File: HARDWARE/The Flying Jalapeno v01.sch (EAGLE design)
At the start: 79 parts, among them J1 ., J2 7V, Q1 8/16MHz, Q2 NPN, Q3 P-Channel MOSFET, Q4 NPN, Q5 P-Channel MOSFET, U1 ATMEGA328

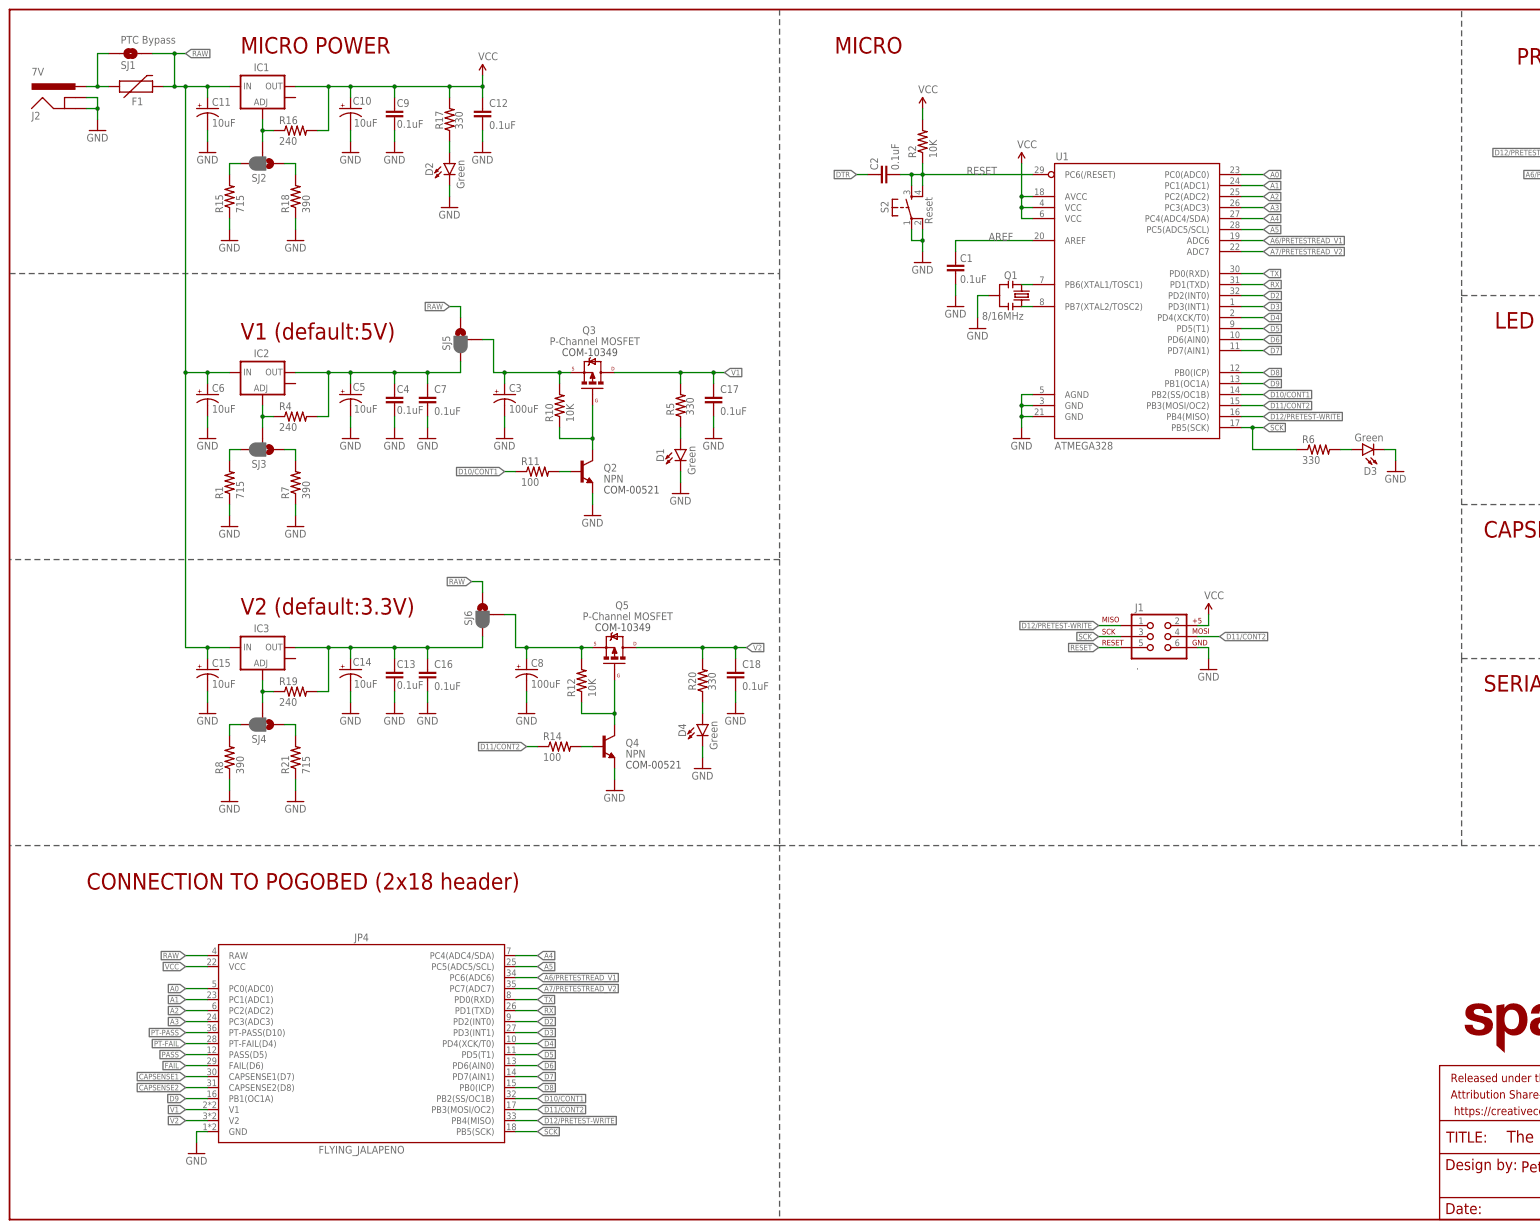
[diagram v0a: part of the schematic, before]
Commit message: Power input Diode
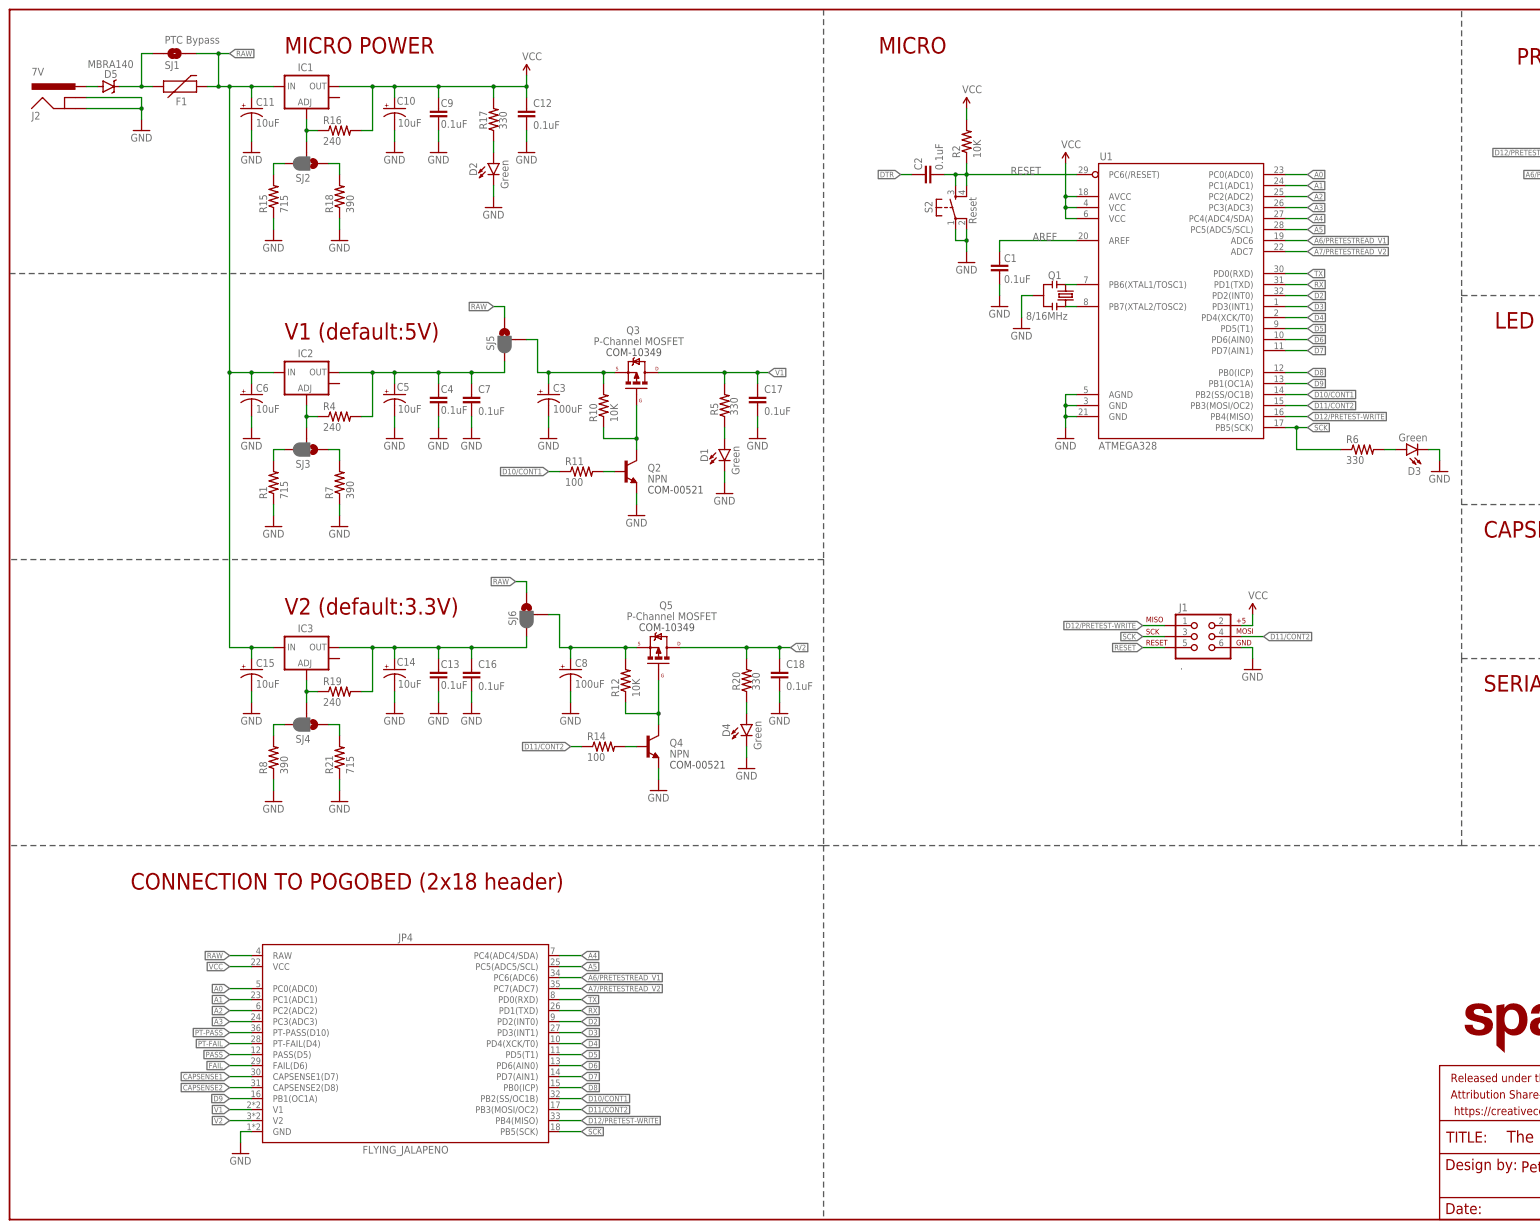
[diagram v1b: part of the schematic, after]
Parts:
- added D5: MBRA140, SparkFun-DiscreteSemi:DIODE-SCHOTTKY-MBRA140
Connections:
- new net N$24: D5.A, J2.PWR
- net N$15: now also D5.C; no longer J2.PWR
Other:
- moved on the sheet: C1, C10, C11, C12, C13, C14, C15, C16, C17, C18, C2, C3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

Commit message: Some PROD_IDS and moved to 100uF SMD caps
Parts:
- C1, C2: device SparkFun-Capacitors:0.1UF-25V-5%(0603) -> SparkFun-Capacitors:0.1UF-25V(+80/-20%)(0603)
- C10, C11, C14, C15, C5, C6: device SparkFun:CAP_POL1206 -> SparkFun-Capacitors:10UF-16V-10%(TANT)
- C12, C13, C16, C17, C18, C4, C7, C9: device SparkFun:CAP0603-CAP -> SparkFun-Capacitors:0.1UF-25V(+80/-20%)(0603)
- C3, C8: device SparkFun-Capacitors:CAP_POLPTH1 -> SparkFun-Capacitors:100UF-63V-20%(ELECT)
- J2: device SparkFun:POWER_JACKPTH_LOCK -> SparkFun-Connectors:POWER_JACKPTH_LOCK
- JP1: device SparkFun:ARDUINO_SERIAL_PROGRAMSMD -> SparkFun-Connectors:ARDUINO_SERIAL_PROGRAMSMD
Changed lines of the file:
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@@
 <part name="S2" library="SparkFun" deviceset="TAC_SWITCH" device="SMD" value="Reset"/>
 <part name="GND3" library="SparkFun" deviceset="GND" device=""/>
-<part name="C1" library="SparkFun-Capacitors" deviceset="0.1UF-25V-5%(0603)" device="" value="0.1uF"/>
+<part name="C1" library="SparkFun-Capacitors" deviceset="0.1UF-25V(+80/-20%)(0603)" device="" value="0.1uF"/>
 <part name="GND7" library="SparkFun" deviceset="GND" device=""/>
 <part name="R6" library="SparkFun-Resistors" deviceset="330OHM1/10W1%(0603)" device="" value="330"/>
@@
 <part name="P+1" library="SparkFun" deviceset="3.3V" device="" value="VCC"/>
 <part name="GND5" library="SparkFun" deviceset="GND" device=""/>
-<part name="JP1" library="SparkFun" deviceset="ARDUINO_SERIAL_PROGRAM" device="SMD" value="FTDI Basic"/>
-<part name="C2" library="SparkFun-Capacitors" deviceset="0.1UF-25V-5%(0603)" device="" value="0.1uF"/>
+<part name="JP1" library="SparkFun-Connectors" deviceset="ARDUINO_SERIAL_PROGRAM" device="SMD" value="FTDI Basic"/>
+<part name="C2" library="SparkFun-Capacitors" deviceset="0.1UF-25V(+80/-20%)(0603)" device="" value="0.1uF"/>
 <part name="JP5" library="SparkFun" deviceset="FIDUCIAL" device="UFIDUCIAL"/>
 <part name="J1" library="SparkFun" deviceset="AVR_SPI_PRG_6" device="2X3_LOCK" value="."/>
@@
 <part name="GND15" library="SparkFun" deviceset="GND" device=""/>
 <part name="Q3" library="Testing" deviceset="MOSFET-PCHANNEL" device="PTH" value="P-Channel MOSFET"/>
-<part name="C3" library="SparkFun-Capacitors" deviceset="CAP_POL" device="PTH1" value="100uF"/>
+<part name="C3" library="SparkFun-Capacitors" deviceset="100UF-63V-20%(ELECT)" device="" value="100uF"/>
 <part name="GND16" library="SparkFun" deviceset="GND" device=""/>
 <part name="Q4" library="SparkFun" deviceset="TRANSISTOR_NPN" device="SOT23" value="NPN"/>
@@
 <part name="GND17" library="SparkFun" deviceset="GND" device=""/>
 <part name="Q5" library="Testing" deviceset="MOSFET-PCHANNEL" device="PTH" value="P-Channel MOSFET"/>
-<part name="C8" library="SparkFun-Capacitors" deviceset="CAP_POL" device="PTH1" value="100uF"/>
+<part name="C8" library="SparkFun-Capacitors" deviceset="100UF-63V-20%(ELECT)" device="" value="100uF"/>
 <part name="GND18" library="SparkFun" deviceset="GND" device=""/>
 <part name="FRAME1" library="SparkFun-Aesthetics" deviceset="FRAME-LEDGER" device=""/>
 <part name="F1" library="Testing" deviceset="PTC" device="WIDE" value=""/>
-<part name="J2" library="SparkFun" deviceset="POWER_JACK" device="PTH_LOCK" value="7V"/>
+<part name="J2" library="SparkFun-Connectors" deviceset="POWER_JACK" device="PTH_LOCK" value="7V"/>
 <part name="GND19" library="SparkFun" deviceset="GND" device=""/>
 <part name="SJ1" library="SparkFun-Passives" deviceset="JUMPER-PAD-2-NO" device="" value="PTC Bypass"/>
 <part name="GND20" library="SparkFun" deviceset="GND" device=""/>
 <part name="P+3" library="SparkFun" deviceset="3.3V" device="" value="VCC"/>
-<part name="C9" library="SparkFun" deviceset="CAP" device="0603-CAP" value="0.1uF"/>
-<part name="C10" library="SparkFun" deviceset="CAP_POL" device="1206" value="10uF"/>
+<part name="C9" library="SparkFun-Capacitors" deviceset="0.1UF-25V(+80/-20%)(0603)" device="" value="0.1uF"/>
+<part name="C10" library="SparkFun-Capacitors" deviceset="10UF-16V-10%(TANT)" device="" value="10uF"/>
 <part name="GND21" library="SparkFun" deviceset="GND" device=""/>
 <part name="GND22" library="SparkFun" deviceset="GND" device=""/>
 <part name="P+5" library="SparkFun" deviceset="VCC" device=""/>
-<part name="C11" library="SparkFun" deviceset="CAP_POL" device="1206" value="10uF"/>
+<part name="C11" library="SparkFun-Capacitors" deviceset="10UF-16V-10%(TANT)" device="" value="10uF"/>
 <part name="IC1" library="SparkFun" deviceset="V_REG_LM1117" device="SOT223"/>
 <part name="R15" library="SparkFun" deviceset="RESISTOR" device="0603-RES" value="715"/>
@@
 <part name="R17" library="SparkFun-Resistors" deviceset="330OHM1/10W1%(0603)" device="" value="330"/>
 <part name="R18" library="SparkFun-Resistors" deviceset="390OHM1/10W1%(0603)" device="" value="390"/>
-<part name="C12" library="SparkFun" deviceset="CAP" device="0603-CAP" value="0.1uF"/>
+<part name="C12" library="SparkFun-Capacitors" deviceset="0.1UF-25V(+80/-20%)(0603)" device="" value="0.1uF"/>
 <part name="GND25" library="SparkFun" deviceset="GND" device=""/>
 <part name="SJ2" library="SparkFun-Passives" deviceset="JUMPER-PAD-3-2OF3_NC_BY_PASTE" device="" value=""/>
 <part name="GND26" library="SparkFun" deviceset="GND" device=""/>
 <part name="GND27" library="SparkFun" deviceset="GND" device=""/>
-<part name="C4" library="SparkFun" deviceset="CAP" device="0603-CAP" value="0.1uF"/>
-<part name="C5" library="SparkFun" deviceset="CAP_POL" device="1206" value="10uF"/>
+<part name="C4" library="SparkFun-Capacitors" deviceset="0.1UF-25V(+80/-20%)(0603)" device="" value="0.1uF"/>
+<part name="C5" library="SparkFun-Capacitors" deviceset="10UF-16V-10%(TANT)" device="" value="10uF"/>
 <part name="GND2" library="SparkFun" deviceset="GND" device=""/>
 <part name="GND6" library="SparkFun" deviceset="GND" device=""/>
-<part name="C6" library="SparkFun" deviceset="CAP_POL" device="1206" value="10uF"/>
+<part name="C6" library="SparkFun-Capacitors" deviceset="10UF-16V-10%(TANT)" device="" value="10uF"/>
 <part name="IC2" library="SparkFun" deviceset="V_REG_LM1117" device="SOT223"/>
 <part name="R1" library="SparkFun" deviceset="RESISTOR" device="0603-RES" value="715"/>
@@
 <part name="R5" library="SparkFun-Resistors" deviceset="330OHM1/10W1%(0603)" device="" value="330"/>
 <part name="R7" library="SparkFun-Resistors" deviceset="390OHM1/10W1%(0603)" device="" value="390"/>
-<part name="C7" library="SparkFun" deviceset="CAP" device="0603-CAP" value="0.1uF"/>
+<part name="C7" library="SparkFun-Capacitors" deviceset="0.1UF-25V(+80/-20%)(0603)" device="" value="0.1uF"/>
 <part name="GND11" library="SparkFun" deviceset="GND" device=""/>
 <part name="SJ3" library="SparkFun-Passives" deviceset="JUMPER-PAD-3-2OF3_NC_BY_PASTE" device="" value=""/>
 <part name="GND12" library="SparkFun" deviceset="GND" device=""/>
 <part name="GND13" library="SparkFun" deviceset="GND" device=""/>
-<part name="C13" library="SparkFun" deviceset="CAP" device="0603-CAP" value="0.1uF"/>
-<part name="C14" library="SparkFun" deviceset="CAP_POL" device="1206" value="10uF"/>
+<part name="C13" library="SparkFun-Capacitors" deviceset="0.1UF-25V(+80/-20%)(0603)" device="" value="0.1uF"/>
+<part name="C14" library="SparkFun-Capacitors" deviceset="10UF-16V-10%(TANT)" device="" value="10uF"/>
 <part name="GND28" library="SparkFun" deviceset="GND" device=""/>
 <part name="GND29" library="SparkFun" deviceset="GND" device=""/>
-<part name="C15" library="SparkFun" deviceset="CAP_POL" device="1206" value="10uF"/>
+<part name="C15" library="SparkFun-Capacitors" deviceset="10UF-16V-10%(TANT)" device="" value="10uF"/>
 <part name="IC3" library="SparkFun" deviceset="V_REG_LM1117" device="SOT223"/>
 <part name="R8" library="SparkFun" deviceset="RESISTOR" device="0603-RES" value="390"/>
@@
 <part name="R20" library="SparkFun-Resistors" deviceset="330OHM1/10W1%(0603)" device="" value="330"/>
 <part name="R21" library="SparkFun-Resistors" deviceset="390OHM1/10W1%(0603)" device="" value="715"/>
-<part name="C16" library="SparkFun" deviceset="CAP" device="0603-CAP" value="0.1uF"/>
+<part name="C16" library="SparkFun-Capacitors" deviceset="0.1UF-25V(+80/-20%)(0603)" device="" value="0.1uF"/>
 <part name="GND32" library="SparkFun" deviceset="GND" device=""/>
 <part name="SJ4" library="SparkFun-Passives" deviceset="JUMPER-PAD-3-2OF3_NC_BY_PASTE" device="" value=""/>
@@
 <part name="GND35" library="SparkFun" deviceset="GND" device=""/>
 <part name="LOGO1" library="SparkFun-Aesthetics" deviceset="SFE_LOGO_NAME_FLAME" device=".5_INCH" value="SFE_LOGO_NAME_FLAME.5_INCH"/>
-<part name="C17" library="SparkFun" deviceset="CAP" device="0603-CAP" value="0.1uF"/>
+<part name="C17" library="SparkFun-Capacitors" deviceset="0.1UF-25V(+80/-20%)(0603)" device="" value="0.1uF"/>
 <part name="GND36" library="SparkFun" deviceset="GND" device=""/>
-<part name="C18" library="SparkFun" deviceset="CAP" device="0603-CAP" value="0.1uF"/>
+<part name="C18" library="SparkFun-Capacitors" deviceset="0.1UF-25V(+80/-20%)(0603)" device="" value="0.1uF"/>
 <part name="GND37" library="SparkFun" deviceset="GND" device=""/>
 <part name="LOGO3" library="SparkFun-Aesthetics" deviceset="SFE_LOGO_FLAME" device=".1_INCH"/>

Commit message: more PROD_IDs
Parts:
- removed S2: Reset, SparkFun:TAC_SWITCHSMD
- removed U1: ATMEGA328, SparkFun:ATMEGA168
- added S1: SWITCH-MOMENTARY-2SMD-REDUNDANT, SparkFun-Electromechanical:SWITCH-MOMENTARY-2SMD-REDUNDANT
- added U2: ATMEGA328P_TQFP, SparkFun-DigitalIC:ATMEGA328P_TQFP
- D1, D2, D3, D4: value Green -> RED; device SparkFun-LED:LED1206 -> SparkFun-LED:LED-RED1206
- F1: value PTCWIDE -> PTCTHERMISTOR1206; device Testing:PTCWIDE -> SparkFun-PowerIC:PTCTHERMISTOR1206
- IC1, IC2, IC3: device SparkFun:V_REG_LM1117SOT223 -> SparkFun-PowerIC:V_REG_LM1117SOT223
- Q1: value 8/16MHz -> 16MHZ; device Testing:RESONATOR1:1 -> SparkFun-FreqCtrl:RESONATOR16MHZ
- Q2, Q4: value NPN -> MMBT2222A; device SparkFun:TRANSISTOR_NPNSOT23 -> SparkFun-DiscreteSemi:TRANSISTOR_NPNMMBT2222A
- R1, R15: device SparkFun:RESISTOR0603-RES -> SparkFun-Resistors:715OHM1/10W1%(0603)
- R10, R12: device SparkFun:RESISTOR0603-RES -> SparkFun-Resistors:10KOHM-1/10W-1%(0603)0603
- R11, R14: device SparkFun:RESISTOR0603-RES -> SparkFun-Resistors:100OHM-1/10W-1%(0603)
- R13, R28, R3, R30: device Testing:RESISTOR0603-RES -> SparkFun-Resistors:10KOHM-1/10W-1%(0603)0603
- R16, R19, R4: device SparkFun:RESISTOR0603-RES -> SparkFun-Resistors:240OHM1/10W1%(0603)
- R17, R20, R22, R23, R24, R25, R5, R6: value 330 -> 390; device SparkFun-Resistors:330OHM1/10W1%(0603) -> SparkFun-Resistors:390OHM1/10W1%(0603)
- R2: device SparkFun-Resistors:10KOHM1/10W1%(0603)0603 -> SparkFun-Resistors:10KOHM-1/10W-1%(0603)0603
- R21: device SparkFun-Resistors:390OHM1/10W1%(0603) -> SparkFun-Resistors:715OHM1/10W1%(0603)
- R26, R27: value 20M -> 22M ohm
- R29, R9: value 100K -> 100k; device Testing:RESISTOR0603-RES -> SparkFun-Resistors:100KOHM-1/10W-1%(0603)
- R8: device SparkFun:RESISTOR0603-RES -> SparkFun-Resistors:390OHM1/10W1%(0603)
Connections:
- removed net N$25: C13.1, C14.+, C16.1, IC3.OUT, R19.2, SJ6.3
- new net VREG2OUT: C13.1, C14.+, C16.1, IC3.OUT, IC3.OUT@1, R19.2, SJ6.3
- net A0: now also U2.PC0(ADC0); no longer U1.PC0(ADC0)
- net A1: now also U2.PC1(ADC1); no longer U1.PC1(ADC1)
- net A2: now also U2.PC2(ADC2); no longer U1.PC2(ADC2)
- net A3: now also U2.PC3(ADC3); no longer U1.PC3(ADC3)
- net A4: now also U2.PC4(ADC4/SDA); no longer U1.PC4(ADC4/SDA)
- net A5: now also U2.PC5(ADC5/SCL); no longer U1.PC5(ADC5/SCL)
- net A6/PRETESTREAD_V1: now also U2.ADC6; no longer U1.ADC6
- net A7/PRETESTREAD_V2: now also U2.ADC7; no longer U1.ADC7
- net AREF: now also U2.AREF; no longer U1.AREF
- net D10/CONT1: now also U2.PB2(SS/OC1B); no longer U1.PB2(SS/OC1B)
- net D11/CONT2: now also U2.PB3(MOSI/OC2); no longer U1.PB3(MOSI/OC2)
- net D12/PRETEST-WRITE: now also U2.PB4(MISO); no longer U1.PB4(MISO)
- net D2: now also U2.PD2(INT0); no longer U1.PD2(INT0)
- net D3: now also U2.PD3(INT1); no longer U1.PD3(INT1)
- net D4: now also U2.PD4(XCK/T0); no longer U1.PD4(XCK/T0)
- net D5: now also U2.PD5(T1); no longer U1.PD5(T1)
- net D6: now also U2.PD6(AIN0); no longer U1.PD6(AIN0)
- net D7: now also U2.PD7(AIN1); no longer U1.PD7(AIN1)
- net D8: now also U2.PB0(ICP); no longer U1.PB0(ICP)
- net D9: now also U2.PB1(OC1A); no longer U1.PB1(OC1A)
- net GND: now also S1.1, U2.AGND, U2.GND@3, U2.GND@5; no longer S2.1, S2.2, U1.AGND, U1.GND@1, U1.GND@2
- net N$1: now also U2.PB7(XTAL2/TOSC2); no longer U1.PB7(XTAL2/TOSC2)
- net N$2: now also U2.PB6(XTAL1/TOSC1); no longer U1.PB6(XTAL1/TOSC1)
- net N$21: now also IC2.OUT@1
- net RESET: now also S1.2, U2.PC6(/RESET); no longer S2.3, S2.4, U1.PC6(/RESET)
- net RX: now also U2.PD1(TXD); no longer U1.PD1(TXD)
- net SCK: now also U2.PB5(SCK); no longer U1.PB5(SCK)
- net TX: now also U2.PD0(RXD); no longer U1.PD0(RXD)
- net VCC: now also IC1.OUT@1, U2.AVCC, U2.VCC@4, U2.VCC@6; no longer U1.AVCC, U1.VCC@1, U1.VCC@2
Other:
- note added: "RES-11132"
- note added: "TRANS-13060"
- note removed: "COM-00521"
- note removed: "COM-10349"
